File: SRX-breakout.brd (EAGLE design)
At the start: 30 x 19.1 mm, 9 parts

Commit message: Updated mechanical drawing of SRX
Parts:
- added U$1: (no value), Stormbots:TALONSRX
- moved QUADRATURE 3.59 mm to (44.5, 8.89)
- moved R1 3.59 mm to (33.0, 16.5)
- moved R2 3.59 mm to (33.0, 14.7)
- moved SJ1 3.59 mm to (30.2, 19.8)
- moved ANALOG_IN 3.59 mm to (36.8, 17.8)
- moved REV_LIMIT 3.59 mm to (36.8, 15.2)
- moved U$2 3.59 mm to (48.3, 14.6)
- moved FWD_LIMIT 3.59 mm to (36.8, 20.3)
- moved QUAD_INDEX 3.59 mm to (36.8, 12.7)
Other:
- board size 30 x 19.1 mm -> 30 x 19 mm

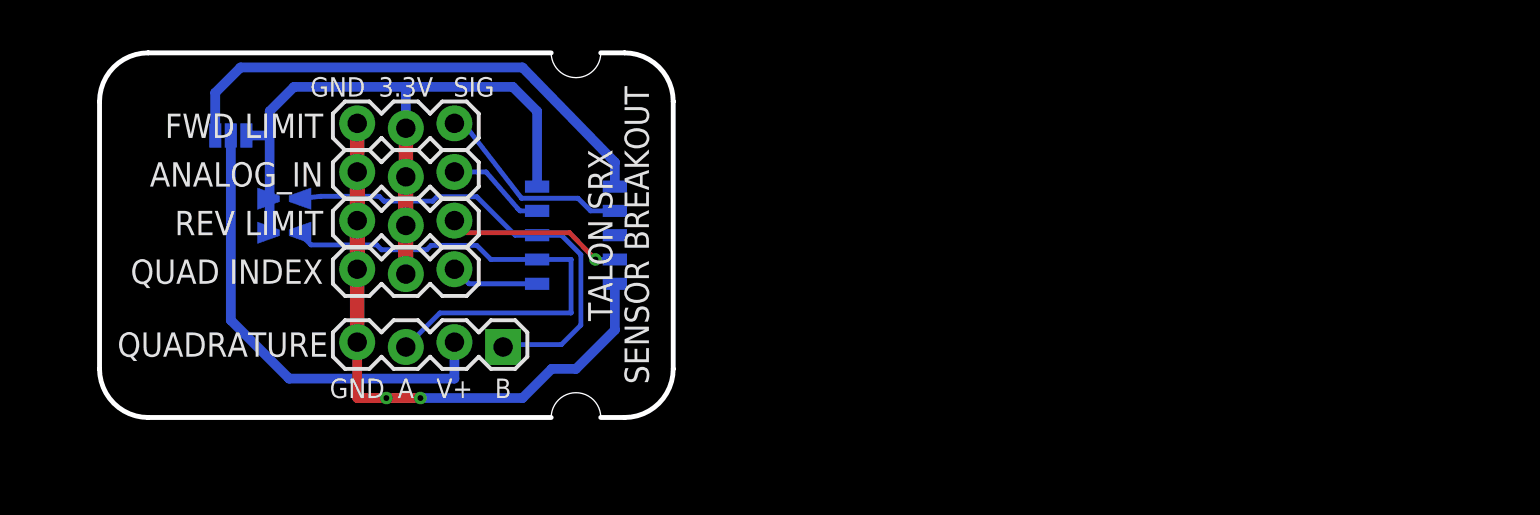
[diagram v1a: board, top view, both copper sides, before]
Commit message: Add CAN subboard
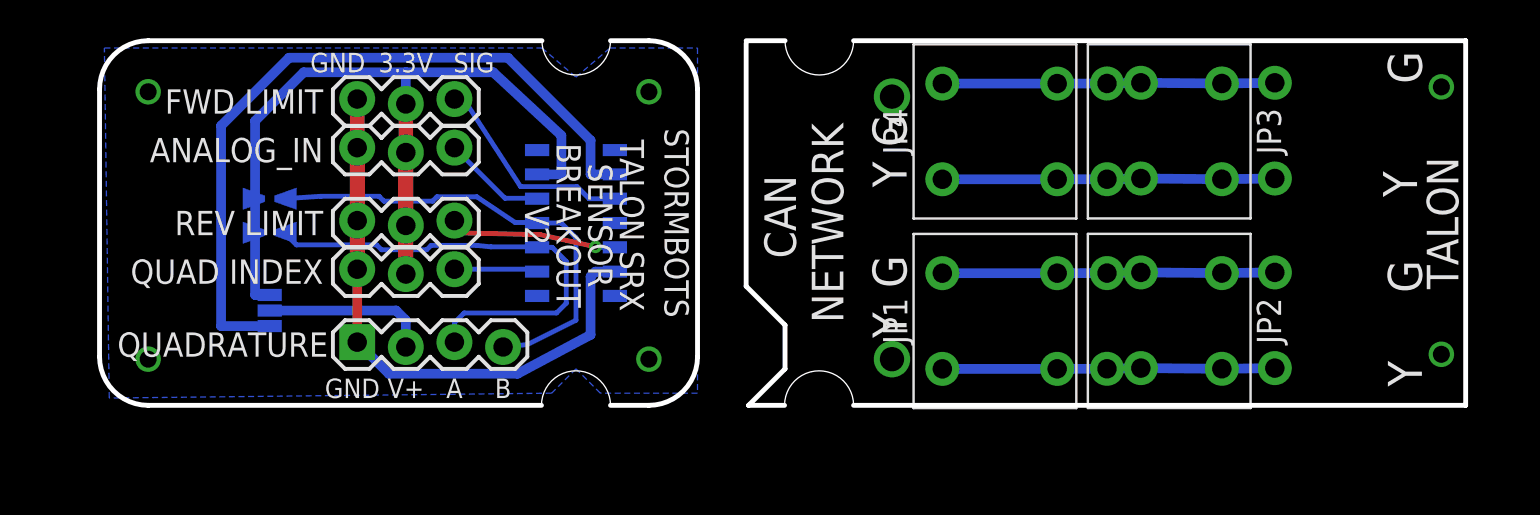
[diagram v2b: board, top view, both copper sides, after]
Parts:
- removed U$2: M05X0250MIL, tekdemo:M2X05_SMD_0.05IN
- added JP1, JP2, JP3, JP4: M022.5MM-SPRING-TERM-VERTICAL, tekdemo:1824740000-2X-VERTICAL-SPRING-TERMINAL
- added JP5, JP6: M022.5MM-SPRING-TERM, tekdemo:1824740000-2X-STRAIGHT-SPRING-TERMINAL
- added U$3: M07X0220021321-00014TFLF, tekdemo:M2X07_SMD
- moved SJ1 9.37 mm to (32.3, 10.7), turned to 90 degrees
- moved QUADRATURE 7.62 mm to (36.8, 8.89), turned to 0 degrees
- moved ANALOG_IN 1.27 mm to (36.8, 19.1)
- moved FWD_LIMIT 1.27 mm to (36.8, 21.6)
- moved R1 0.76 mm to (32.3, 16.5)
- moved R2 0.76 mm to (32.3, 14.7)
- moved U$1 0.66 mm to (48.3, 15.3)
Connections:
- net N$1 renamed QUAD_VOLTAGE
- new net N$1: JP3.2A, JP3.2B, JP4.1A, JP4.1B, JP6.2A, JP6.2B
- new net N$6: JP3.1A, JP3.1B, JP4.2A, JP4.2B, JP6.1A, JP6.1B
- new net N$7: JP1.1A, JP1.1B, JP2.2A, JP2.2B, JP5.2A, JP5.2B
- new net N$8: JP1.2A, JP1.2B, JP2.1A, JP2.1B, JP5.1A, JP5.1B
- net 3.3V: now also U$3.P$13; no longer U$2.P$10
- net 5V: now also U$3.P$2; no longer U$2.P$1
- net ANALOG_IN: now also U$3.P$12; no longer U$2.P$9
- net FWD_LIMIT: now also U$3.P$3; no longer U$2.P$2
- net GND: now also QUADRATURE.1, U$3.P$6; no longer QUADRATURE.4, U$2.P$5
- net NC: now also U$3.P$4; no longer U$2.P$3
- net QUADA: now also U$3.P$10; no longer U$2.P$7
- net QUADB: now also QUADRATURE.4, U$3.P$11; no longer QUADRATURE.1, U$2.P$8
- net QUADINDEX: now also U$3.P$9; no longer U$2.P$6
- net REV_LIMIT: now also U$3.P$5; no longer U$2.P$4
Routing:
- net N$8: track 0.00 -> 17.4 mm
- net N$7: track 0.00 -> 17.4 mm
- net N$6: track 0.00 -> 17.4 mm
- net N$1: track 0.00 -> 17.4 mm
- net QUAD_VOLTAGE: track 24.5 -> 8.72 mm
- net 5V: track 27.0 -> 38.6 mm
- net 3.3V: track 44.7 -> 52.2 mm
- net GND: track 43.6 -> 40.8 mm, vias 2 -> 0
- net QUADA: track 27.2 -> 25.0 mm
- net FWD_LIMIT: track 10.6 -> 11.1 mm
- net REV_LIMIT: track 9.61 -> 9.10 mm
- added copper zone on layer 16, net NC
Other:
- board size 30 x 19 mm -> 71.4 x 19.1 mm
- board text added: "CAN NETWORK"
- board text added: "G"
- board text added: "SRX"
- board text added: "TALON"
- board text added: "TALON SRX SENSOR BREAKOUT V2"
- board text added: "TAPE BOTTOM TO PREVENT SHORTS"
- board text added: "WIRE"
- board text added: "Y"
- board text removed: "TALON SRX SENSOR BREAKOUT"
- board text removed: "TAPE BOTTOM OF BOARD TO PREVENT SHORTS ON CHASSIS"

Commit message: Minor adjustments for mechanical purposes
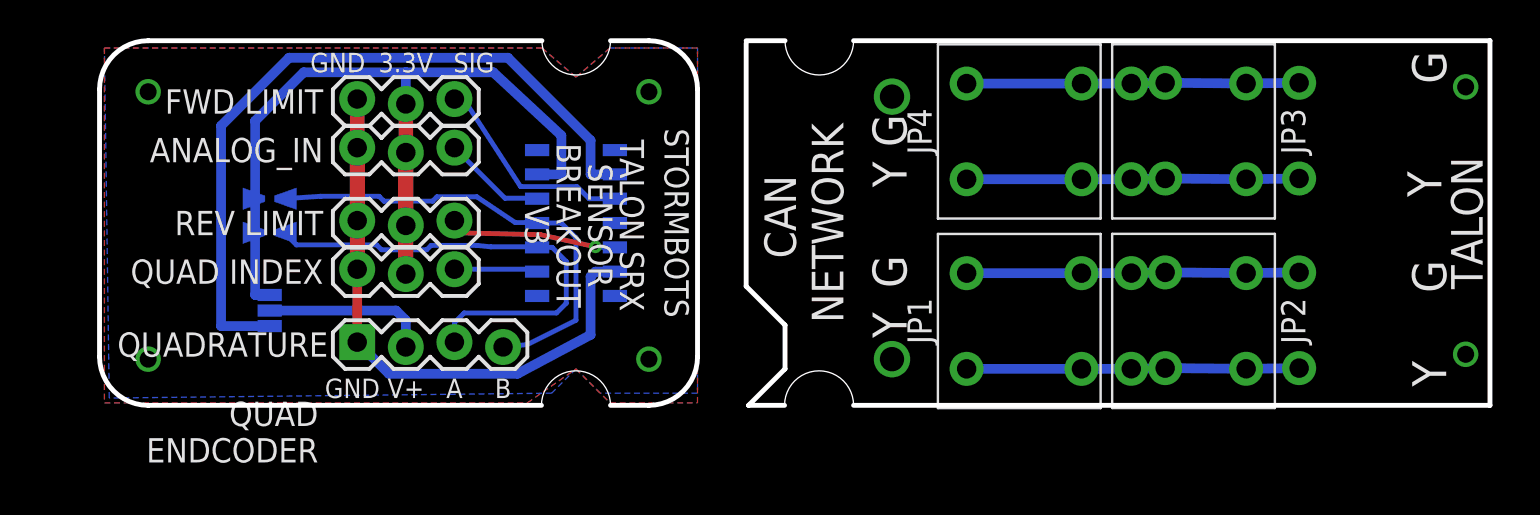
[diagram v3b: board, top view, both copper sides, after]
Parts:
- moved JP2 1.27 mm to (77.3, 12.6)
- moved JP3 1.27 mm to (77.3, 22.5)
- moved JP1 1.27 mm to (74.7, 7.62)
- moved JP4 1.27 mm to (74.7, 17.5)
- moved JP5 1.27 mm to (82.0, 10.2)
- moved JP6 1.27 mm to (82.0, 20.1)
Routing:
- added copper zone on layer 1, net N$13
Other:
- board size 71.4 x 19.1 mm -> 72.6 x 19.1 mm
- board text added: "QUAD ENDCODER"
- board text added: "SRX CAN BREAKOUT V3"
- board text added: "TALON SRX SENSOR BREAKOUT V3"
- board text removed: "TALON SRX SENSOR BREAKOUT V2"
